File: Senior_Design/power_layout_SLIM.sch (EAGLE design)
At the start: 36 parts, among them IC1 MIC29302WU, J1[SIMCARD] 78646-3001, J2 292303-1, J3[GROVE] 640456-4, J4[GROVE] 640456-4, U1 SIM7000E, U2 TUSB2046BIRHBR

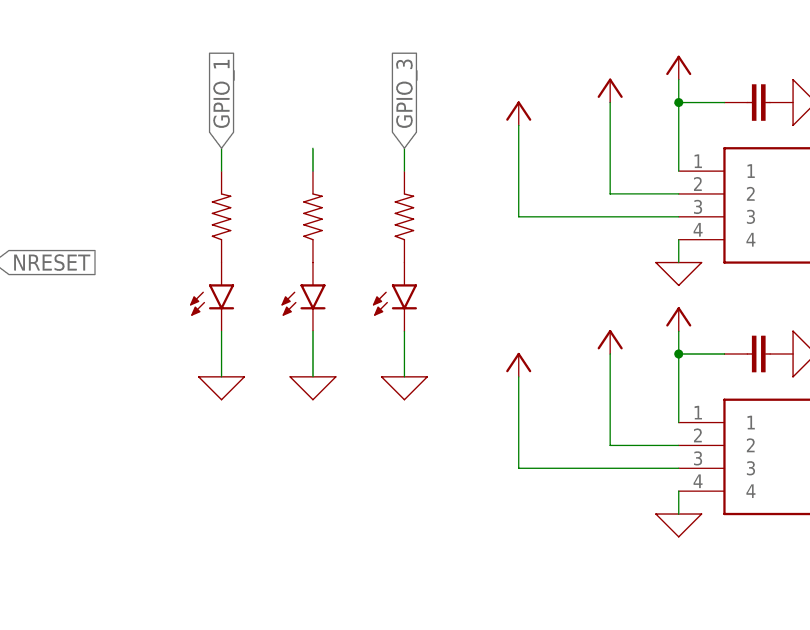
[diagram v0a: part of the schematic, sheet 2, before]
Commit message: Add files via upload
Upload at beginning of pre-CDR work.  Minimal changes since April (addition of UART level shifter for sim7000)
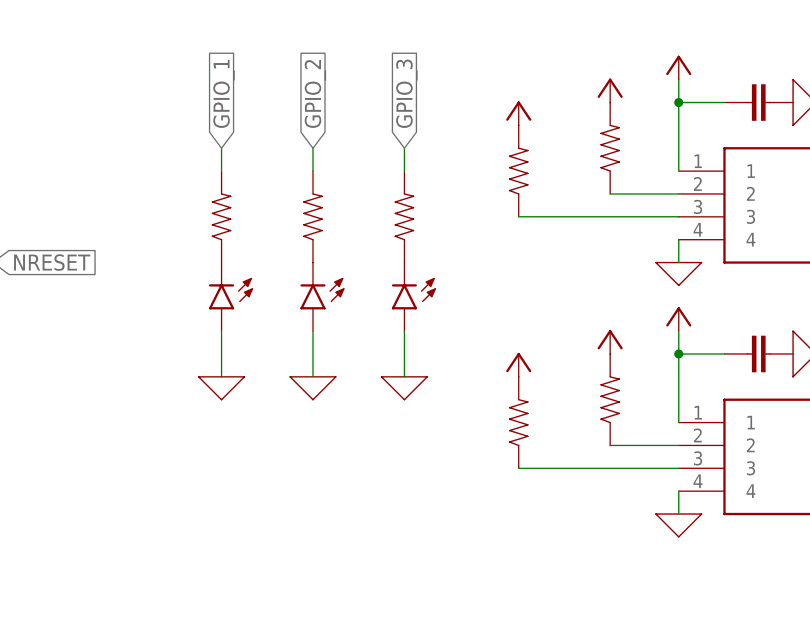
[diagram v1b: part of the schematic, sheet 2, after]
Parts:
- added R11, R12, R7, R8: (no value), SparkFun-Resistors:RESISTOR0402
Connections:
- net N$9 renamed GPIO_2
- new net N$10: J3[GROVE].3, R8.1
- new net N$12: J4[GROVE].2, R11.1
- new net N$13: J4[GROVE].3, R12.1
- new net N$9: J3[GROVE].2, R7.1
- net +5V: now also R11.2, R12.2, R7.2, R8.2; no longer J3[GROVE].2, J3[GROVE].3, J4[GROVE].2, J4[GROVE].3
- net 0: now also D1.A, D2.A, D3.A; no longer D1.C, D2.C, D3.C
- net N$5: now also D3.C; no longer D3.A
- net N$7: now also D2.C; no longer D2.A
- net N$8: now also D1.C; no longer D1.A
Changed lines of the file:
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@@
 <part name="R5" library="SparkFun-Resistors" library_urn="urn:adsk.eagle:library:532" deviceset="RESISTOR" device="0402" package3d_urn="urn:adsk.eagle:package:39657/1" value=" "/>
 <part name="R6" library="SparkFun-Resistors" library_urn="urn:adsk.eagle:library:532" deviceset="RESISTOR" device="0402" package3d_urn="urn:adsk.eagle:package:39657/1" value=" "/>
+<part name="R7" library="SparkFun-Resistors" library_urn="urn:adsk.eagle:library:532" deviceset="RESISTOR" device="0402" package3d_urn="urn:adsk.eagle:package:39657/1" value=" "/>
 <part name="P+3" library="supply1" library_urn="urn:adsk.eagle:library:371" deviceset="+5V" device=""/>
+<part name="R8" library="SparkFun-Resistors" library_urn="urn:adsk.eagle:library:532" deviceset="RESISTOR" device="0402" package3d_urn="urn:adsk.eagle:package:39657/1" value=" "/>
 <part name="P+4" library="supply1" library_urn="urn:adsk.eagle:library:371" deviceset="+5V" device=""/>
 <part name="X_14" library="ngspice-simulation" library_urn="urn:adsk.eagle:library:527439" deviceset="GND" device=""/>
@@
 <part name="BRD1" library="e14_BeagleBoard_PocketBeagle_v1_alpha1" deviceset="POCKETBEAGLE_?_2" device="BRD"/>
 <part name="J4[GROVE]" library="640456-4" deviceset="640456-4" device=""/>
+<part name="R11" library="SparkFun-Resistors" library_urn="urn:adsk.eagle:library:532" deviceset="RESISTOR" device="0402" package3d_urn="urn:adsk.eagle:package:39657/1" value=" "/>
 <part name="P+8" library="supply1" library_urn="urn:adsk.eagle:library:371" deviceset="+5V" device=""/>
+<part name="R12" library="SparkFun-Resistors" library_urn="urn:adsk.eagle:library:532" deviceset="RESISTOR" device="0402" package3d_urn="urn:adsk.eagle:package:39657/1" value=" "/>
 <part name="P+9" library="supply1" library_urn="urn:adsk.eagle:library:371" deviceset="+5V" device=""/>
 <part name="X_22" library="ngspice-simulation" library_urn="urn:adsk.eagle:library:527439" deviceset="GND" device=""/>
@@
 <instance part="R5" gate="G$1" x="83.82" y="27.94" smashed="yes" rot="R90" grouprefs="POWER"/>
 <instance part="R6" gate="G$1" x="99.06" y="27.94" smashed="yes" rot="R90" grouprefs="POWER"/>
-<instance part="D1" gate="G$1" x="88.9" y="78.74" smashed="yes" grouprefs="USER_IO"/>
-<instance part="D2" gate="G$1" x="99.06" y="78.74" smashed="yes" grouprefs="USER_IO"/>
-<instance part="D3" gate="G$1" x="109.22" y="78.74" smashed="yes" grouprefs="USER_IO"/>
+<instance part="D1" gate="G$1" x="88.9" y="76.2" smashed="yes" rot="R180" grouprefs="USER_IO"/>
+<instance part="D2" gate="G$1" x="99.06" y="76.2" smashed="yes" rot="R180" grouprefs="USER_IO"/>
+<instance part="D3" gate="G$1" x="109.22" y="76.2" smashed="yes" rot="R180" grouprefs="USER_IO"/>
 <instance part="X_10" gate="G$1" x="109.22" y="68.58" smashed="yes" rot="MR0" grouprefs="USER_IO"/>
 <instance part="X_11" gate="G$1" x="99.06" y="68.58" smashed="yes" rot="MR0" grouprefs="USER_IO"/>
@@
 <instance part="P+12" gate="1" x="55.88" y="104.14" smashed="yes" grouprefs="USER_IO"/>
 <instance part="J3[GROVE]" gate="G$1" x="149.86" y="86.36" smashed="yes" grouprefs="GROVE"/>
+<instance part="R7" gate="G$1" x="132.08" y="93.98" smashed="yes" rot="R90" grouprefs="GROVE"/>
 <instance part="P+3" gate="1" x="132.08" y="101.6" smashed="yes" grouprefs="GROVE"/>
+<instance part="R8" gate="G$1" x="121.92" y="91.44" smashed="yes" rot="R90" grouprefs="GROVE"/>
 <instance part="P+4" gate="1" x="121.92" y="99.06" smashed="yes" grouprefs="GROVE"/>
 <instance part="X_14" gate="G$1" x="139.7" y="81.28" smashed="yes" rot="MR0" grouprefs="GROVE"/>
@@
 <instance part="X_15" gate="G$1" x="152.4" y="99.06" smashed="yes" rot="MR270" grouprefs="GROVE"/>
 <instance part="J4[GROVE]" gate="G$1" x="149.86" y="58.42" smashed="yes" grouprefs="GROVE"/>
+<instance part="R11" gate="G$1" x="132.08" y="66.04" smashed="yes" rot="R90" grouprefs="GROVE"/>
 <instance part="P+8" gate="1" x="132.08" y="73.66" smashed="yes" grouprefs="GROVE"/>
+<instance part="R12" gate="G$1" x="121.92" y="63.5" smashed="yes" rot="R90" grouprefs="GROVE"/>
 <instance part="P+9" gate="1" x="121.92" y="71.12" smashed="yes" grouprefs="GROVE"/>
 <instance part="X_22" gate="G$1" x="139.7" y="53.34" smashed="yes" rot="MR0" grouprefs="GROVE"/>
@@
 </segment>
 <segment>
+<pinref part="D1" gate="G$1" pin="A"/>
+<pinref part="X_12" gate="G$1" pin="0"/>
+<wire x1="88.9" y1="73.66" x2="88.9" y2="68.58" width="0.1524" layer="91" grouprefs="USER_IO"/>
+</segment>
+<segment>
+<pinref part="D2" gate="G$1" pin="A"/>
+<pinref part="X_11" gate="G$1" pin="0"/>
+<wire x1="99.06" y1="73.66" x2="99.06" y2="68.58" width="0.1524" layer="91" grouprefs="USER_IO"/>
+</segment>
+<segment>
+<pinref part="D3" gate="G$1" pin="A"/>
+<pinref part="X_10" gate="G$1" pin="0"/>
+<wire x1="109.22" y1="73.66" x2="109.22" y2="68.58" width="0.1524" layer="91" grouprefs="USER_IO"/>
+</segment>
+<segment>
 <pinref part="R10" gate="G$1" pin="1"/>
 <pinref part="X_16" gate="G$1" pin="0"/>
@@
 <pinref part="C7" gate="G$1" pin="1"/>
 <pinref part="X_23" gate="G$1" pin="0"/>
-</segment>
-<segment>
-<pinref part="D1" gate="G$1" pin="C"/>
-<pinref part="X_12" gate="G$1" pin="0"/>
-<wire x1="88.9" y1="73.66" x2="88.9" y2="68.58" width="0.1524" layer="91"/>
-</segment>
-<segment>
-<pinref part="X_11" gate="G$1" pin="0"/>
-<pinref part="D2" gate="G$1" pin="C"/>
-<wire x1="99.06" y1="73.66" x2="99.06" y2="68.58" width="0.1524" layer="91"/>
-</segment>
-<segment>
-<pinref part="X_10" gate="G$1" pin="0"/>
-<pinref part="D3" gate="G$1" pin="C"/>
-<wire x1="109.22" y1="73.66" x2="109.22" y2="68.58" width="0.1524" layer="91"/>
 </segment>
 </net>
@@
 </segment>
 <segment>
+<pinref part="R7" gate="G$1" pin="2"/>
+<pinref part="P+3" gate="1" pin="+5V"/>
+</segment>
+<segment>
+<pinref part="R8" gate="G$1" pin="2"/>
+<pinref part="P+4" gate="1" pin="+5V"/>
+</segment>
+<segment>
 <pinref part="J3[GROVE]" gate="G$1" pin="1"/>
 <wire x1="139.7" y1="91.44" x2="139.7" y2="99.06" width="0.1524" layer="91" grouprefs="GROVE"/>
@@
 </segment>
 <segment>
+<pinref part="R11" gate="G$1" pin="2"/>
+<pinref part="P+8" gate="1" pin="+5V"/>
+</segment>
+<segment>
+<pinref part="R12" gate="G$1" pin="2"/>
+<pinref part="P+9" gate="1" pin="+5V"/>
+</segment>
+<segment>
 <pinref part="J4[GROVE]" gate="G$1" pin="1"/>
 <wire x1="139.7" y1="63.5" x2="139.7" y2="71.12" width="0.1524" layer="91" grouprefs="GROVE"/>
@@
 <pinref part="C7" gate="G$1" pin="2"/>
 </segment>
-<segment>
-<pinref part="J3[GROVE]" gate="G$1" pin="3"/>
-<wire x1="139.7" y1="86.36" x2="121.92" y2="86.36" width="0.1524" layer="91" grouprefs="GROVE"/>
-<pinref part="P+4" gate="1" pin="+5V"/>
-<wire x1="121.92" y1="96.52" x2="121.92" y2="86.36" width="0.1524" layer="91"/>
-</segment>
-<segment>
-<pinref part="J3[GROVE]" gate="G$1" pin="2"/>
-<wire x1="139.7" y1="88.9" x2="132.08" y2="88.9" width="0.1524" layer="91" grouprefs="GROVE"/>
-<pinref part="P+3" gate="1" pin="+5V"/>
-<wire x1="132.08" y1="99.06" x2="132.08" y2="88.9" width="0.1524" layer="91"/>
-</segment>
-<segment>
-<pinref part="J4[GROVE]" gate="G$1" pin="3"/>
-<wire x1="139.7" y1="58.42" x2="121.92" y2="58.42" width="0.1524" layer="91" grouprefs="GROVE"/>
-<pinref part="P+9" gate="1" pin="+5V"/>
-<wire x1="121.92" y1="58.42" x2="121.92" y2="68.58" width="0.1524" layer="91"/>
-</segment>
-<segment>
-<pinref part="J4[GROVE]" gate="G$1" pin="2"/>
-<wire x1="139.7" y1="60.96" x2="132.08" y2="60.96" width="0.1524" layer="91" grouprefs="GROVE"/>
-<pinref part="P+8" gate="1" pin="+5V"/>
-<wire x1="132.08" y1="60.96" x2="132.08" y2="71.12" width="0.1524" layer="91"/>
+</net>
+<net name="N$7" class="0">
+<segment>
+<pinref part="D2" gate="G$1" pin="C"/>
+<pinref part="R2" gate="G$1" pin="1"/>
+</segment>
+</net>
+<net name="N$5" class="0">
+<segment>
+<pinref part="D3" gate="G$1" pin="C"/>
+<pinref part="R1" gate="G$1" pin="1"/>
+</segment>
+</net>
+<net name="N$8" class="0">
+<segment>
+<pinref part="D1" gate="G$1" pin="C"/>
+<pinref part="R3" gate="G$1" pin="1"/>
 </segment>
 </net>
@@
 </segment>
 </net>
+<net name="GPIO_2" class="0">
+<segment>
+<pinref part="R2" gate="G$1" pin="2"/>
+<wire x1="99.06" y1="91.44" x2="99.06" y2="93.98" width="0.1524" layer="91" grouprefs="USER_IO"/>
+<label x="99.06" y="93.98" size="1.778" layer="95" rot="R90" xref="yes" grouprefs="USER_IO"/>
+</segment>
+</net>
 <net name="GPIO_1" class="0">
 <segment>
@@
 </segment>
 </net>
-<net name="N$8" class="0">
-<segment>
-<pinref part="D1" gate="G$1" pin="A"/>
-<pinref part="R3" gate="G$1" pin="1"/>
-</segment>
-</net>
-<net name="N$7" class="0">
-<segment>
-<pinref part="D2" gate="G$1" pin="A"/>
-<pinref part="R2" gate="G$1" pin="1"/>
-</segment>
-</net>
 <net name="N$9" class="0">
 <segment>
-<pinref part="R2" gate="G$1" pin="2"/>
-<wire x1="99.06" y1="91.44" x2="99.06" y2="93.98" width="0.1524" layer="91"/>
-</segment>
-</net>
-<net name="N$5" class="0">
-<segment>
-<pinref part="R1" gate="G$1" pin="1"/>
-<pinref part="D3" gate="G$1" pin="A"/>
-</segment>
-</net>
+<pinref part="J3[GROVE]" gate="G$1" pin="2"/>
+<pinref part="R7" gate="G$1" pin="1"/>
+<wire x1="139.7" y1="88.9" x2="132.08" y2="88.9" width="0.1524" layer="91" grouprefs="GROVE"/>
+</segment>
+</net>
+<net name="N$10" class="0">
+<segment>
+<pinref part="J3[GROVE]" gate="G$1" pin="3"/>
+<wire x1="139.7" y1="86.36" x2="121.92" y2="86.36" width="0.1524" layer="91" grouprefs="GROVE"/>
+<pinref part="R8" gate="G$1" pin="1"/>
+</segment>
+</net>
+<net name="N$12" class="0">
+<segment>
+<pinref part="J4[GROVE]" gate="G$1" pin="2"/>
+<pinref part="R11" gate="G$1" pin="1"/>
+<wire x1="139.7" y1="60.96" x2="132.08" y2="60.96" width="0.1524" layer="91" grouprefs="GROVE"/>
+</segment>
+</net>
+<net name="N$13" class="0">
+<segment>
+<pinref part="J4[GROVE]" gate="G$1" pin="3"/>
+<wire x1="139.7" y1="58.42" x2="121.92" y2="58.42" width="0.1524" layer="91" grouprefs="GROVE"/>
+<pinref part="R12" gate="G$1" pin="1"/>
+</segment>
+</net>
